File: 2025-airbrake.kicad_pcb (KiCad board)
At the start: 2 copper layers, 88.7 x 58.2 mm, 11 parts, among them J1 SERVO, J2 JST-DY, J3 POWER_SEL, U1 STM32F411 Black Pill, U2 SPI Flash W25Q128JV, U3 Adafruit Micro SD Breakout, U4 MS5611, U5 NeoPixel Stick, U6 BNO055 Breakout, U7 MP2307 EVAL, U8 RFD900X

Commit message: Routing
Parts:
- U7: footprint Connector_PinHeader_2.54mm:PinHeader_2x02_P2.54mm_Vertical -> Connector_PinHeader_2.54mm:PinHeader_1x03_P2.54mm_Vertical
- moved U7 8.04 mm to (174.0, 71.1), turned to 180 degrees
- moved J3 5.08 mm to (163.2, 66.0), turned to 0 degrees
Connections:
- U1 pad 14: unconnected-(U1-PB0-Pad14) -> /BNO_RST
- U1 pad 18: unconnected-(U1-3V3-Pad18) -> +3V3
- U1 pad 34: /CS-SD -> unconnected-(U1-PB6-Pad34)
- U1 pad 35: /CS-FLASH -> unconnected-(U1-PB7-Pad35)
- U1 pad 38: +5V -> unconnected-(U1-5V-Pad38)
- U1 pad 40: +3V3 -> unconnected-(U1-3V3-Pad40)
- U1 pad 6: unconnected-(U1-PA0-Pad6) -> /CS-SD
- U1 pad 9: unconnected-(U1-PA3-Pad9) -> /CS-FLASH
- U6 pad 6: unconnected-(U6-RST-Pad6) -> /BNO_RST
- U7 pad 1: +5V -> GND
- U7 pad 2: GND -> +5V
- U7 pad 3: GND -> +BATT
- U8 pad 5: unconnected-(U8-VUSB-Pad5) -> +5V
- U8 pad 6: unconnected-(U8-VUSB-Pad6) -> +5V
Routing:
- net +5V: track 144.9 -> 93.4 mm, vias 1 -> 0
- net /BNO_RST: track 0.00 -> 28.8 mm
- net /RX: track 79.5 -> 61.9 mm, vias 1 -> 0
- net /SCL: track 79.9 -> 94.8 mm
- net /TX: track 73.5 -> 58.8 mm, vias 1 -> 0
- net +3V3: track 112.5 -> 101.2 mm
- net /CS-SD: track 31.4 -> 20.9 mm
- net +BATT: track 26.3 -> 24.9 mm
- net /SCK: track 43.5 -> 44.9 mm
- net /NEO-DATA: track 25.3 -> 26.7 mm
- net /PWM: track 26.7 -> 26.0 mm, vias 1 -> 0
- net /CS-FLASH: track 50.1 -> 50.6 mm
- net /MISO: track 46.6 -> 47.0 mm, vias 2 -> 0
- net /MOSI: track 48.2 -> 47.8 mm, vias 2 -> 0
- net GND: vias 5 -> 0
- removed copper zone on F.Cu, net GND

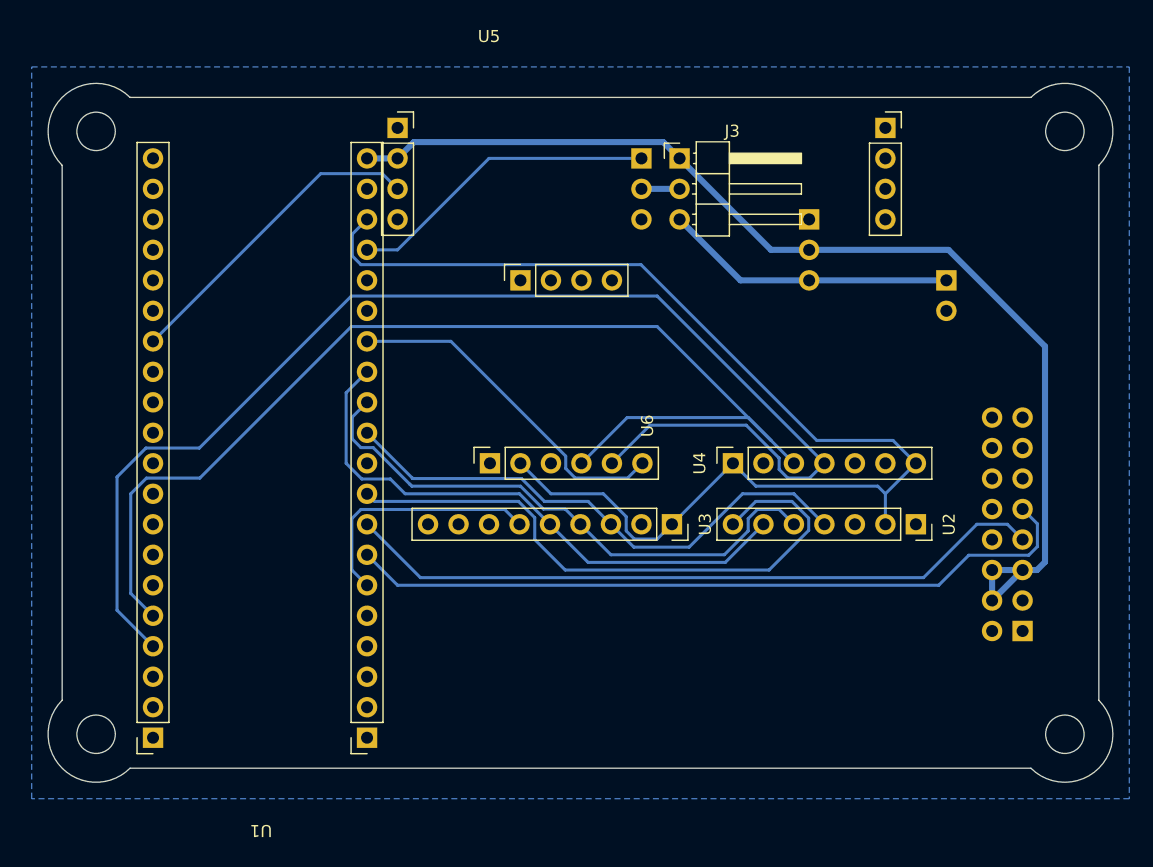
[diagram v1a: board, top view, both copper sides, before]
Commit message: Added symbols and heiarchy
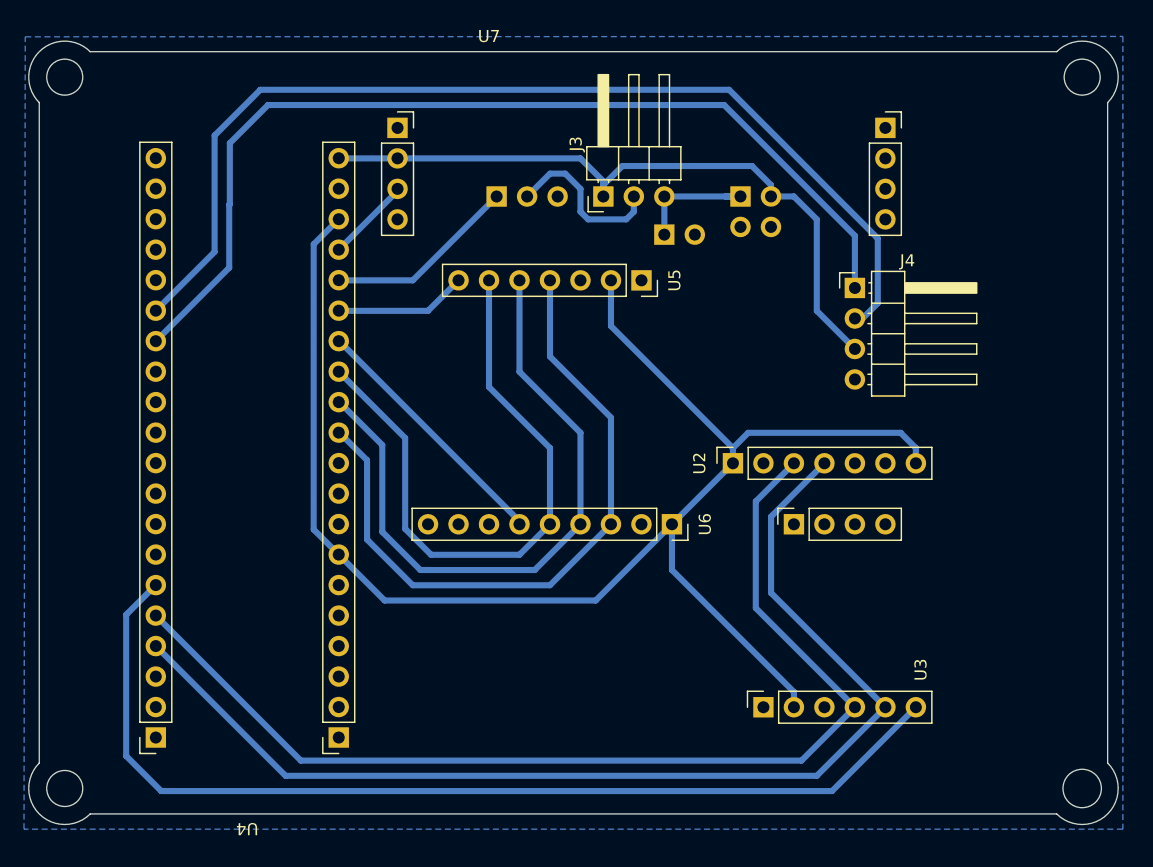
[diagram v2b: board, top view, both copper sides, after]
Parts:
- removed U8: RFD900X, Connector_PinSocket_2.54mm:PinSocket_2x08_P2.54mm_Horizontal
- added J4: RFD900X, Connector_PinHeader_2.54mm:PinHeader_1x04_P2.54mm_Horizontal, F.Cu at (177.8, 76.8)
- U1: renamed from U7; footprint Connector_PinHeader_2.54mm:PinHeader_1x03_P2.54mm_Vertical -> Connector_PinHeader_2.54mm:PinHeader_2x02_P2.54mm_Vertical
- moved U5 30.6 mm to (160.0, 76.2)
- moved U3 30.5 mm to (177.8, 104.1)
- moved J1 23.8 mm to (161.9, 72.4), turned to -90 degrees
- moved J2 12.5 mm to (148.0, 69.2), turned to -90 degrees
- moved J3 7.10 mm to (156.8, 69.2), turned to 90 degrees
- moved U1 6.03 mm to (168.3, 69.2), turned to -90 degrees
- moved U4 1.16 mm to (127.2, 88.9)
- renumbered J2 to J1, J1 to J2, U4 to U2, U6 to U3, U1 to U4, U2 to U5, U3 to U6, U5 to U7
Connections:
- U1 pad 1: GND -> +BATT
- U1 pad 2: +5V -> GND
- U1 pad 3: +BATT -> +5V
- U2 pad 5: unconnected-(U4-CSB-Pad5) -> GND
- U2 pad 6: unconnected-(U4-SDO-Pad6) -> GND
- U4 pad 14: /BNO_RST -> /CS_SD
- U4 pad 15: unconnected-(U1-PB1-Pad15) -> /CS_FLASH
- U4 pad 16: unconnected-(U1-PB2-Pad16) -> /PWM
- U4 pad 17: /PWM -> /NEO_DATA
- U4 pad 2: unconnected-(U1-PC13-Pad2) -> GND
- U4 pad 26: unconnected-(U1-PA9-Pad26) -> /TX
- U4 pad 27: /NEO-DATA -> /RX
- U4 pad 28: unconnected-(U1-PA11-Pad28) -> GND
- U4 pad 3: unconnected-(U1-PC14-Pad3) -> GND
- U4 pad 34: unconnected-(U1-PB6-Pad34) -> GND
- U4 pad 35: unconnected-(U1-PB7-Pad35) -> /BNO_RST
- U4 pad 39: GND -> unconnected-(U4-GND-Pad39)
- U4 pad 6: /CS-SD -> unconnected-(U4-PA0-Pad6)
- U4 pad 7: /RX -> +3V3
- U4 pad 8: /TX -> unconnected-(U4-PA2-Pad8)
- U4 pad 9: /CS-FLASH -> unconnected-(U4-PA3-Pad9)
- U5 pad 7: /CS-FLASH -> /CS_FLASH
- U6 pad 6: /CS-SD -> /CS_SD
- U7 pad 3: /NEO-DATA -> /NEO_DATA
- U7 pad 4: GND -> unconnected-(U7-GND-Pad4)
- U7 pad 5: GND -> unconnected-(U7-GND-Pad5)
- U7 pad 8: GND -> unconnected-(U7-GND-Pad8)
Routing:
- net /BNO_RST: track 28.8 -> 85.2 mm
- net /CS-FLASH: track 50.6 -> 0.00 mm
- net +5V: track 93.4 -> 58.2 mm
- net /TX: track 58.8 -> 86.4 mm
- net /NEO-DATA: track 26.7 -> 0.00 mm
- net +3V3: track 101.2 -> 125.2 mm
- net /CS_SD: track 0.00 -> 21.7 mm
- net /CS-SD: track 20.9 -> 0.00 mm
- net /RX: track 61.9 -> 81.3 mm
- net /SDA: track 108.2 -> 93.7 mm
- net +BATT: track 24.9 -> 10.8 mm
- net /SCK: track 44.9 -> 56.5 mm
- net /CS_FLASH: track 0.00 -> 11.2 mm
- net Net-(J2-Pin_2): track 3.23 -> 13.9 mm
- net /PWM: track 26.0 -> 16.2 mm
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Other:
- board size 88.7 x 58.2 mm -> 90.8 x 65.3 mm
